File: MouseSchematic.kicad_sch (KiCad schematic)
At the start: 67 parts, among them IC1 AZ1117IH-3.3TRG1, J1 Right Header, J2 Left Header, J4 JST1, J5 JST2, J6 Programming Header, Q1 IR Receiver, Q2 IR Receiver, Q3 IR Receiver, Q4 IR Receiver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

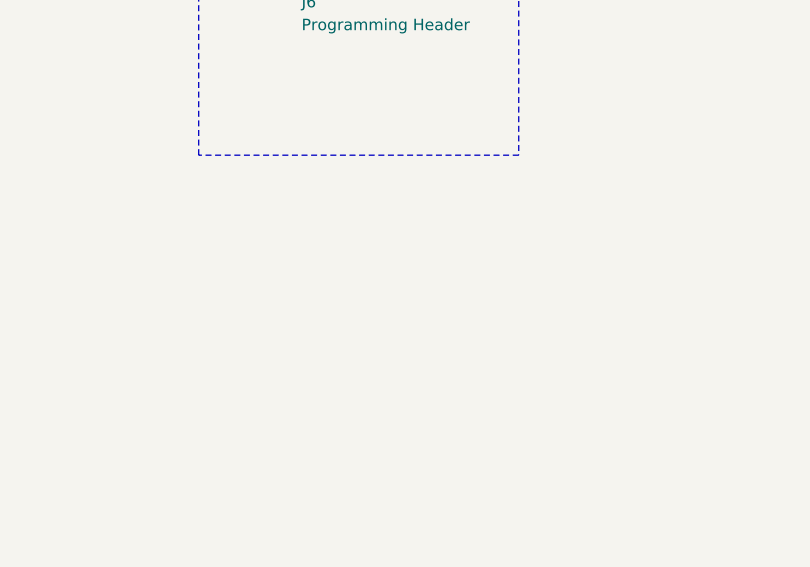
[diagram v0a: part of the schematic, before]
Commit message: Redo main layout and add motor footprints
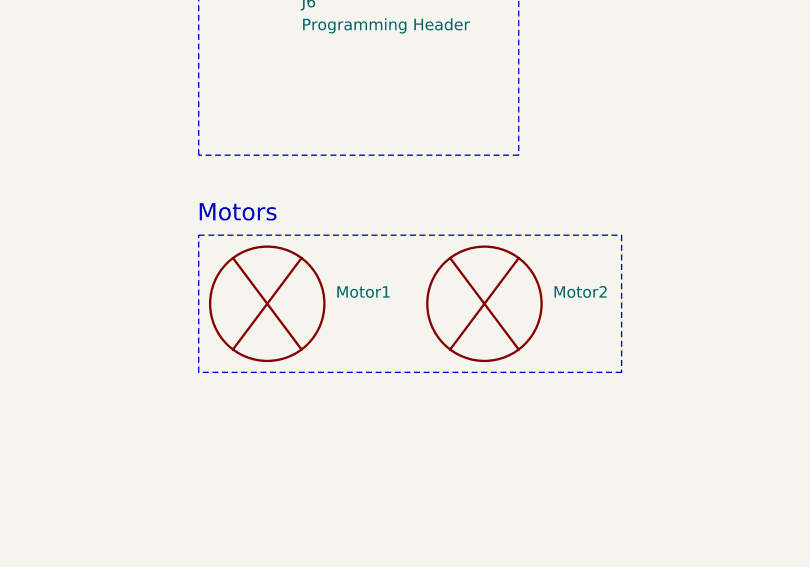
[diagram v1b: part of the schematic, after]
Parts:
- added Motor1, Motor2: ~, Pololu_Motor:Pololu_Motor, symbol Pololu_motor:Pololu_Motor
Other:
- note added: "Motors"
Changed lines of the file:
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@@
 	)
 	(rectangle
+		(start 144.78 138.43)
+		(end 191.77 153.67)
+		(stroke
+			(width 0)
+			(type dash)
+		)
+		(fill
+			(type none)
+		)
+	)
+	(rectangle
 		(start 59.69 111.76)
 		(end 118.11 190.5)
@@
 		)
 	)
+	(text "Motors"
+		(exclude_from_sim no)
+		(at 149.098 136.144 0)
+		(effects
+			(font
+				(size 1.905 1.905)
+			)
+		)
+	)
 	(text "Left IR Emitter"
 		(exclude_from_sim no)
@@
 	)
 	(symbol
+		(lib_id "Pololu_motor:Pololu_Motor")
+		(at 176.53 153.67 0)
+		(unit 1)
+		(exclude_from_sim no)
+		(in_bom yes)
+		(on_board yes)
+		(dnp no)
+		(fields_autoplaced yes)
+		(property "Reference" "Motor2"
+			(at 184.15 144.7799 0)
+			(effects
+				(font
+					(size 1.27 1.27)
+				)
+				(justify left)
+			)
+		)
+		(property "Value" "~"
+			(at 184.15 147.3199 0)
+			(effects
+				(font
+					(size 1.27 1.27)
+				)
+				(justify left)
+			)
+		)
+		(property "Footprint" "Pololu_Motor:Pololu_Motor"
+			(at 176.53 153.67 0)
+			(effects
+				(font
+					(size 1.27 1.27)
+				)
+				(hide yes)
+			)
+		)
+		(property "Datasheet" ""
+			(at 176.53 153.67 0)
+			(effects
+				(font
+					(size 1.27 1.27)
+				)
+				(hide yes)
+			)
+		)
+		(property "Description" ""
+			(at 176.53 153.67 0)
+			(effects
+				(font
+					(size 1.27 1.27)
+				)
+				(hide yes)
+			)
+		)
+		(instances
+			(project "MouseSchematic"
+				(path "/a8212d07-d284-4713-b6f1-5033ff009a76"
+					(reference "Motor2")
+					(unit 1)
+				)
+			)
+		)
+	)
+	(symbol
 		(lib_id "Button_FSM4JSMA:FSM4JSMA")
 		(at 163.83 55.88 270)
@@
 					(unit 1)
 				)
+			)
+		)
+	)
+	(symbol
+		(lib_id "Pololu_motor:Pololu_Motor")
+		(at 152.4 153.67 0)
+		(unit 1)
+		(exclude_from_sim no)
+		(in_bom yes)
+		(on_board yes)
+		(dnp no)
+		(fields_autoplaced yes)
+		(property "Reference" "Motor1"
+			(at 160.02 144.7799 0)
+			(effects
+				(font
+					(size 1.27 1.27)
+				)
+				(justify left)
+			)
+		)
+		(property "Value" "~"
+			(at 160.02 147.3199 0)
+			(effects
+				(font
+					(size 1.27 1.27)
+				)
+				(justify left)
+			)
+		)
+		(property "Footprint" "Pololu_Motor:Pololu_Motor"
+			(at 152.4 153.67 0)
+			(effects
+				(font
+					(size 1.27 1.27)
+				)
+				(hide yes)
+			)
+		)
+		(property "Datasheet" ""
+			(at 152.4 153.67 0)
+			(effects
+				(font
+					(size 1.27 1.27)
+				)
+				(hide yes)
+			)
+		)
+		(property "Description" ""
+			(at 152.4 153.67 0)
+			(effects
+				(font
+					(size 1.27 1.27)
+				)
+				(hide yes)
+			)
+		)
+		(instances
+			(project ""
+				(path "/a8212d07-d284-4713-b6f1-5033ff009a76"
+					(reference "Motor1")
+					(unit 1)
+				)

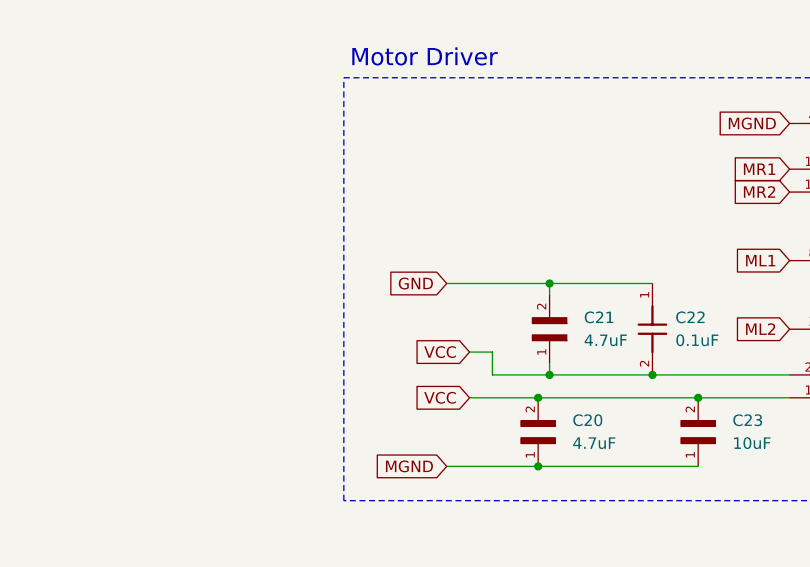
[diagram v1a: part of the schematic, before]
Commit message: Finished PCB with MGND issue fixed and edge cuts for battery holders
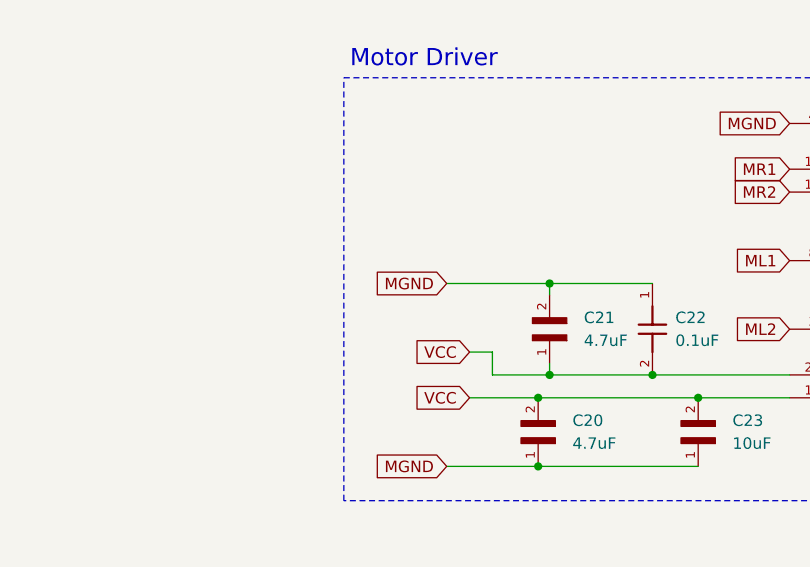
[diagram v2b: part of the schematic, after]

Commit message: Fixed error in schematic with incorrect MGND label
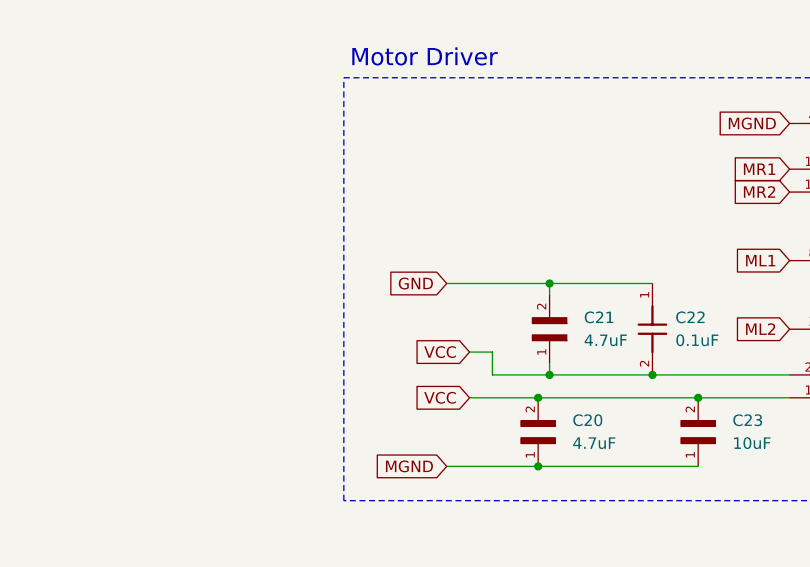
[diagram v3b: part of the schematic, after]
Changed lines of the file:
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@@
 		)
 	)
-	(global_label "MGND"
+	(global_label "GND"
 		(shape input)
 		(at 427.99 140.97 180)
@@
 		)
 		(property "Intersheetrefs" "${INTERSHEET_REFS}"
-			(at 419.6829 140.97 0)
+			(at 421.1343 140.97 0)
 			(effects
 				(font
